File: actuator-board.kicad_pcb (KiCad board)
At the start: 2 copper layers, 60 parts, among them J1 SERVO PWR, M1 Motor_Servo, M2 Motor_Servo, M3 Pump 1, M4 Pump 2, U1 STM32F302K8U6, U2 MCP1703, U3 MAX3051, U4 MPRLS0015PA0000SA, U5 MPRLS0015PA0000SA, U6 DRV8847_TSSOP, X1 16MHz 10ppm

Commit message: Upadate footprints, rough arrangement
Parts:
- removed CONN5: ANALOG2, Connector_Molex:Molex_PicoBlade_53261-0271_1x02-1MP_P1.25mm_Horizontal
- removed CONN6: ANALOG1, Connector_Molex:Molex_PicoBlade_53261-0271_1x02-1MP_P1.25mm_Horizontal
- removed CONN7: Digital input 1, Connector_Molex:Molex_PicoBlade_53261-0271_1x02-1MP_P1.25mm_Horizontal
- removed L1: Solenoid 1, Connector_PinHeader_2.54mm:PinHeader_1x02_P2.54mm_Vertical
- removed L2: Solenoid 2, Connector_PinHeader_2.54mm:PinHeader_1x02_P2.54mm_Vertical
- removed M3: Pump 1, Connector_PinHeader_2.54mm:PinHeader_1x02_P2.54mm_Vertical
- removed M4: Pump 2, Connector_PinHeader_2.54mm:PinHeader_1x02_P2.54mm_Vertical
- added H1: MountingHole, MountingHole:MountingHole_2.2mm_M2, F.Cu at (50.8, 40.4)
- added H2: MountingHole, MountingHole:MountingHole_2.2mm_M2, F.Cu at (51.6, 102.4)
- added H3: MountingHole, MountingHole:MountingHole_2.2mm_M2, F.Cu at (87.6, 42.4)
- added H4: MountingHole, MountingHole:MountingHole_2.2mm_M2, F.Cu at (88.6, 102.6)
- added J2: Conn_01x06, Connector_Molex:Molex_PicoBlade_53261-0671_1x06-1MP_P1.25mm_Horizontal, F.Cu at (67.1, 102.4)
- added J3: Actuator1, Connector_Molex:Molex_PicoBlade_53261-0471_1x04-1MP_P1.25mm_Horizontal, F.Cu at (54.1, 49.8)
- added J4: Actuator2, Connector_Molex:Molex_PicoBlade_53261-0471_1x04-1MP_P1.25mm_Horizontal, F.Cu at (91.2, 50.8)
- C19: footprint Capacitor_THT:CP_Radial_D6.3mm_P2.50mm -> Capacitor_SMD:CP_Elec_5x5.8
- C2, C3, C4, C5, C6, C7, C8: footprint Capacitor_SMD:C_0402_1005Metric -> Capacitor_SMD:C_0603_1608Metric
- CONN3: footprint Connector_Molex:Molex_PicoBlade_53261-0471_1x04-1MP_P1.25mm_Horizontal -> Connector_Molex:Molex_PicoBlade_53398-0471_1x04-1MP_P1.25mm_Vertical
- CONN4: footprint Connector_Molex:Molex_PicoBlade_53261-0471_1x04-1MP_P1.25mm_Horizontal -> Connector_Molex:Molex_PicoBlade_53398-0471_1x04-1MP_P1.25mm_Vertical; moved to F.Cu
- J1: value SERVO PWR -> SERVO DCDC 5V; footprint Connector_PinHeader_2.54mm:PinHeader_1x02_P2.54mm_Vertical -> Connector_PinHeader_2.54mm:PinHeader_1x03_P2.54mm_Vertical
- M1, M2: footprint Connector_PinHeader_2.54mm:PinHeader_1x03_P2.54mm_Horizontal -> Connector_Molex:Molex_PicoBlade_53261-0371_1x03-1MP_P1.25mm_Horizontal
- moved C12 84.3 mm to (111.8, 133.9)
- moved R10 84.3 mm to (110.2, 136.9)
- moved R8 84.3 mm to (104.1, 133.3)
- moved C11 84.3 mm to (100.3, 135.1)
- moved R7 84.3 mm to (103.4, 136.7)
- moved R9 84.3 mm to (115.1, 135.1)
- moved M1 77.2 mm to (52.8, 61.7), turned to 270 degrees
- moved CONN4 64.4 mm to (90.7, 91.7)
- moved M2 60.2 mm to (90.4, 64.0), turned to 90 degrees
- moved C18 59.1 mm to (77.1, 37.2)
- moved D3 59.1 mm to (77.9, 34.3)
- moved D4 59.1 mm to (68.6, 41.5)
- moved D5 59.1 mm to (74.1, 41.5)
- moved R2 59.1 mm to (59.9, 44.6)
- moved C17 59.1 mm to (60.7, 41.7)
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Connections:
- J1 pad 1: Net-(C17-Pad1) -> +BATT

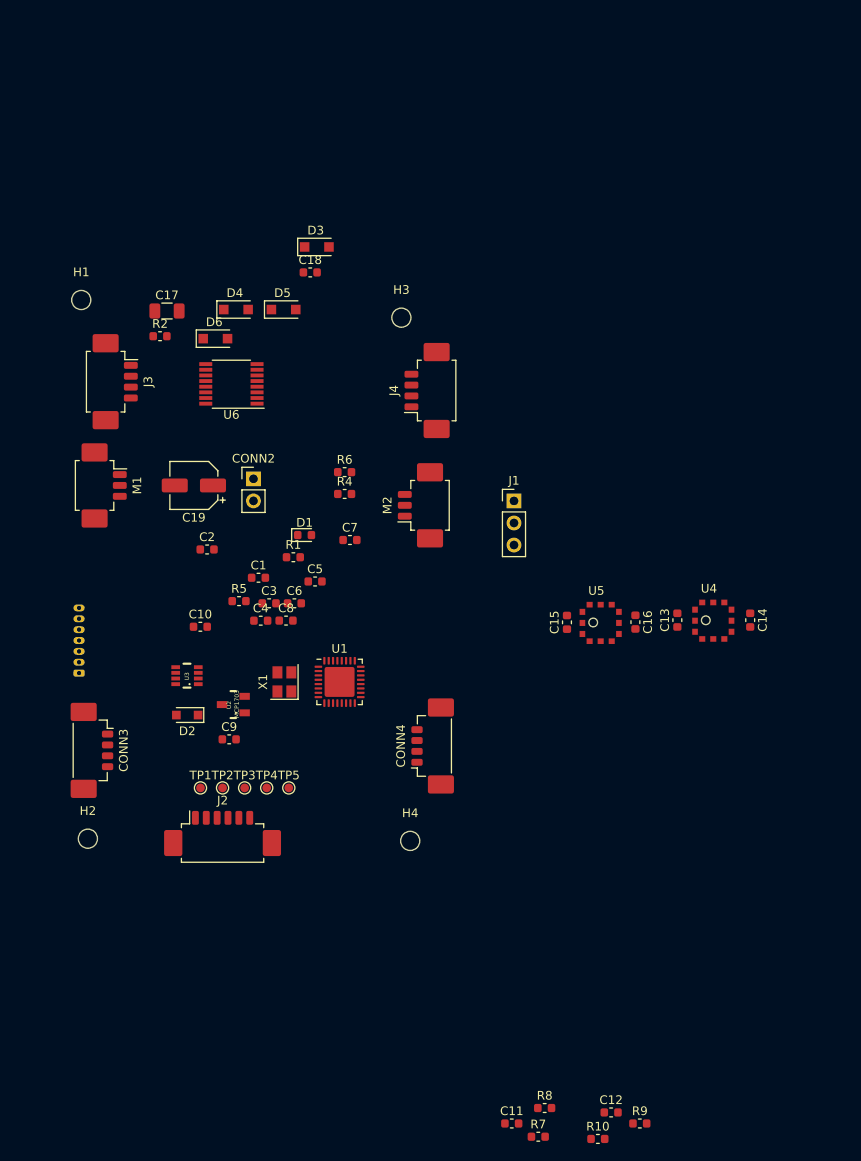
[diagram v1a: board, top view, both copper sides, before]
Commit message: Rough component placement, defined outline
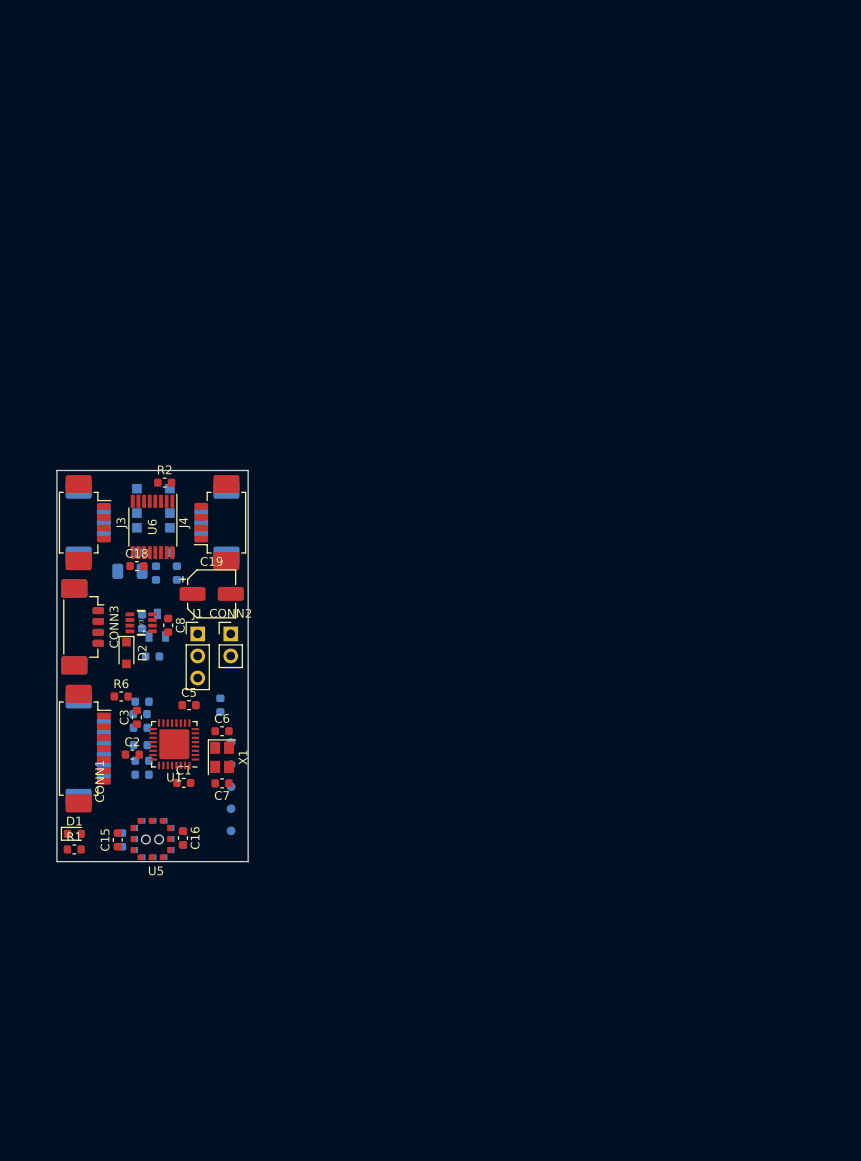
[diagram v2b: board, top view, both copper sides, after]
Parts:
- removed H1, H2, H3, H4: MountingHole, MountingHole:MountingHole_2.2mm_M2
- C10, C11, C12, C13, C14, C17, C4, C9, CONN4, D3, D4, D5, D6, J2, M1, M2, R10, R4, R5, R7, R8, R9, TP1, TP2, TP3, TP4, TP5, U2, U4: moved to B.Cu
- CONN1: footprint Connector_Molex:Molex_PicoBlade_53048-0710_1x07_P1.25mm_Horizontal -> Connector_Molex:Molex_PicoBlade_53261-0771_1x07-1MP_P1.25mm_Horizontal; moved to F.Cu
- moved R9 72.1 mm to (57.6, 91.6)
- moved U4 70.8 mm to (57.0, 104.5)
- moved C14 69.9 mm to (62.5, 102.3), turned to 90 degrees
- moved C13 68.7 mm to (55.5, 102.5), turned to 270 degrees
- moved R10 68.1 mm to (57.8, 93.4), turned to 180 degrees
- moved C12 66.5 mm to (57.8, 95.0), turned to 180 degrees
- moved R8 65.8 mm to (57.8, 86.6), turned to 180 degrees
- moved R7 65.6 mm to (57.6, 89.6), turned to 180 degrees
- moved C11 63.6 mm to (57.6, 88.0), turned to 180 degrees
- moved C16 57.7 mm to (62.5, 102.3)
- moved C15 57.4 mm to (55.0, 102.5)
- moved U5 55.6 mm to (61.0, 104.5), turned to 180 degrees
- moved D1 43.4 mm to (50.0, 101.8)
- moved R1 42.0 mm to (50.0, 103.6)
- moved CONN4 41.5 mm to (51.5, 78.0)
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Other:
- board outline added: 22 x 45 mm

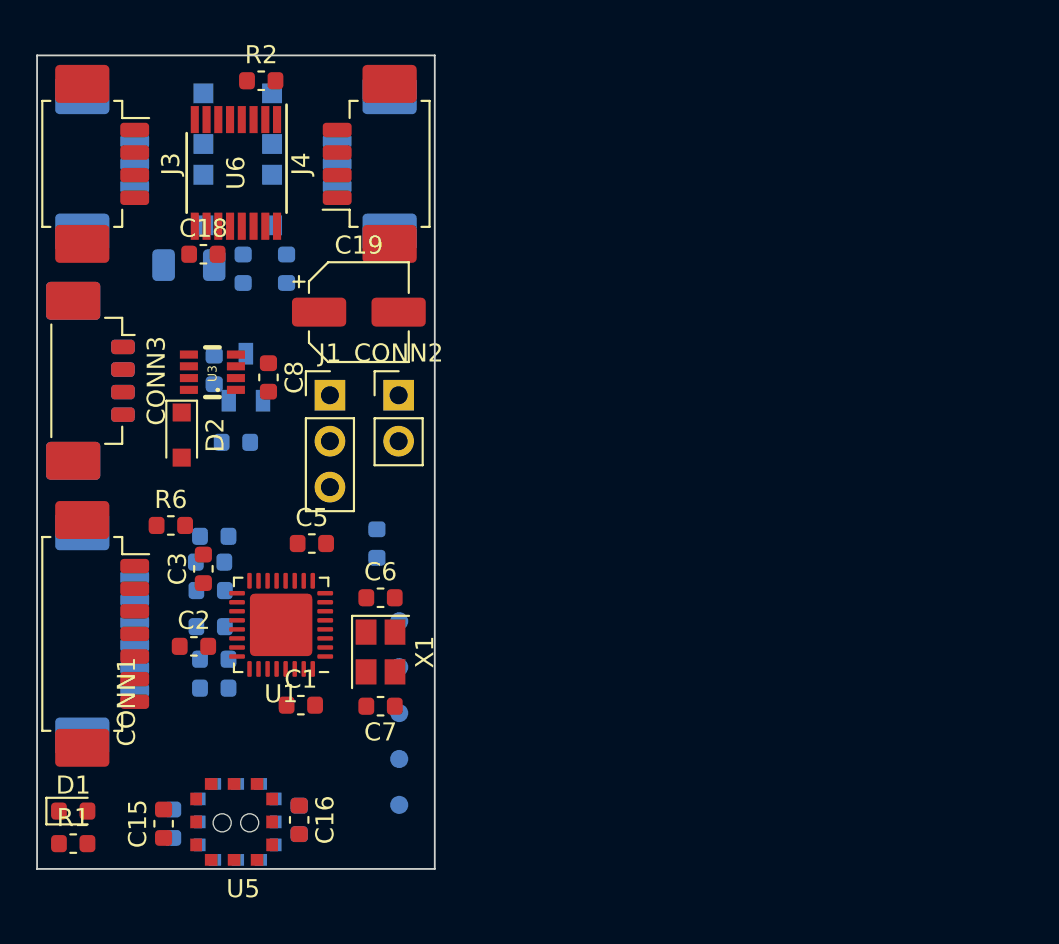
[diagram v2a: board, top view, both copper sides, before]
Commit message: Update footprints, better refdes, cleanup schematic, 40x22mm outline
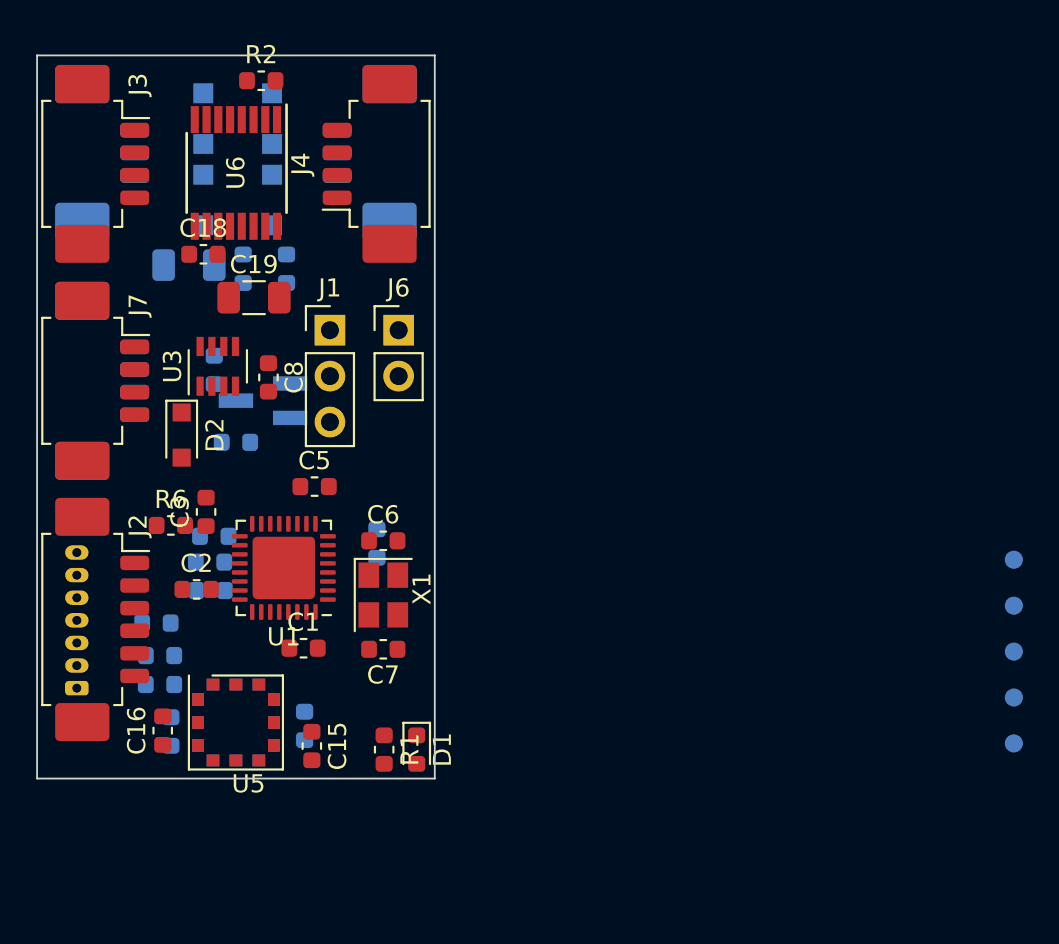
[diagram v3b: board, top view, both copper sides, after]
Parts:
- removed CONN1: SWD/DEBUG, Connector_Molex:Molex_PicoBlade_53261-0771_1x07-1MP_P1.25mm_Horizontal
- removed CONN2: BATTERY, Connector_PinHeader_2.54mm:PinHeader_1x02_P2.54mm_Vertical
- removed CONN3, CONN4: CAN, Connector_Molex:Molex_PicoBlade_53398-0471_1x04-1MP_P1.25mm_Vertical
- removed M1, M2: Motor_Servo, Connector_Molex:Molex_PicoBlade_53261-0371_1x03-1MP_P1.25mm_Horizontal
- added J10: Servo, Connector_Molex:Molex_PicoBlade_53261-0371_1x03-1MP_P1.25mm_Horizontal, B.Cu at (67.0, 65.4)
- added J5: SWD/DEBUG, Connector_Molex:Molex_PicoBlade_53047-0710_1x07_P1.25mm_Vertical, B.Cu at (50.2, 95.0)
- added J6: BATTERY, Connector_PinHeader_2.54mm:PinHeader_1x02_P2.54mm_Vertical, F.Cu at (68.0, 75.2)
- added J7: CAN, Connector_Molex:Molex_PicoBlade_53261-0471_1x04-1MP_P1.25mm_Horizontal, F.Cu at (51.0, 78.0)
- added J8: CAN, Connector_Molex:Molex_PicoBlade_53261-0471_1x04-1MP_P1.25mm_Horizontal, B.Cu at (51.0, 78.0)
- added J9: Servo, Connector_Molex:Molex_PicoBlade_53261-0371_1x03-1MP_P1.25mm_Horizontal, B.Cu at (51.0, 65.4)
- C10: value 22uF -> 1uF
- C18: value 0.1 uF -> 0.1uF
- C19: footprint Capacitor_SMD:CP_Elec_5x5.8 -> Capacitor_SMD:C_1206_3216Metric
- J2: moved to F.Cu
- U2: footprint _div:_MCP1703-SOT-23A -> Package_TO_SOT_SMD:SOT-23_Handsoldering
- U3: footprint _std:_SOT23-8 -> Package_TO_SOT_SMD:SOT-23-8
- U4, U5: footprint _sensors:MPR -> _sensors:MPR-AbsoluteRef
- moved TP1 34.2 mm to (102.0, 98.1)
- moved TP2 34.2 mm to (102.0, 95.5)
- moved TP3 34.2 mm to (102.0, 93.0)
- moved TP4 34.2 mm to (102.0, 90.4)
- moved TP5 34.2 mm to (102.0, 87.9)
- moved D1 19.3 mm to (69.0, 98.4), turned to 270 degrees
- moved R1 18.0 mm to (67.2, 98.4), turned to 270 degrees
- moved C15 9.26 mm to (63.2, 98.2), turned to 270 degrees
- moved C16 9.02 mm to (55.0, 97.3), turned to 90 degrees
- moved C19 5.85 mm to (60.0, 73.4)
- moved U4 5.50 mm to (56.9, 99.0)
- moved U5 5.50 mm to (61.1, 99.0)
- moved C14 5.21 mm to (62.8, 97.1)
- moved C13 5.10 mm to (55.4, 97.4)
- moved J1 3.60 mm to (64.2, 75.2)
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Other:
- board size 22 x 45 mm -> 22 x 40 mm
- copper layers 2 -> 4

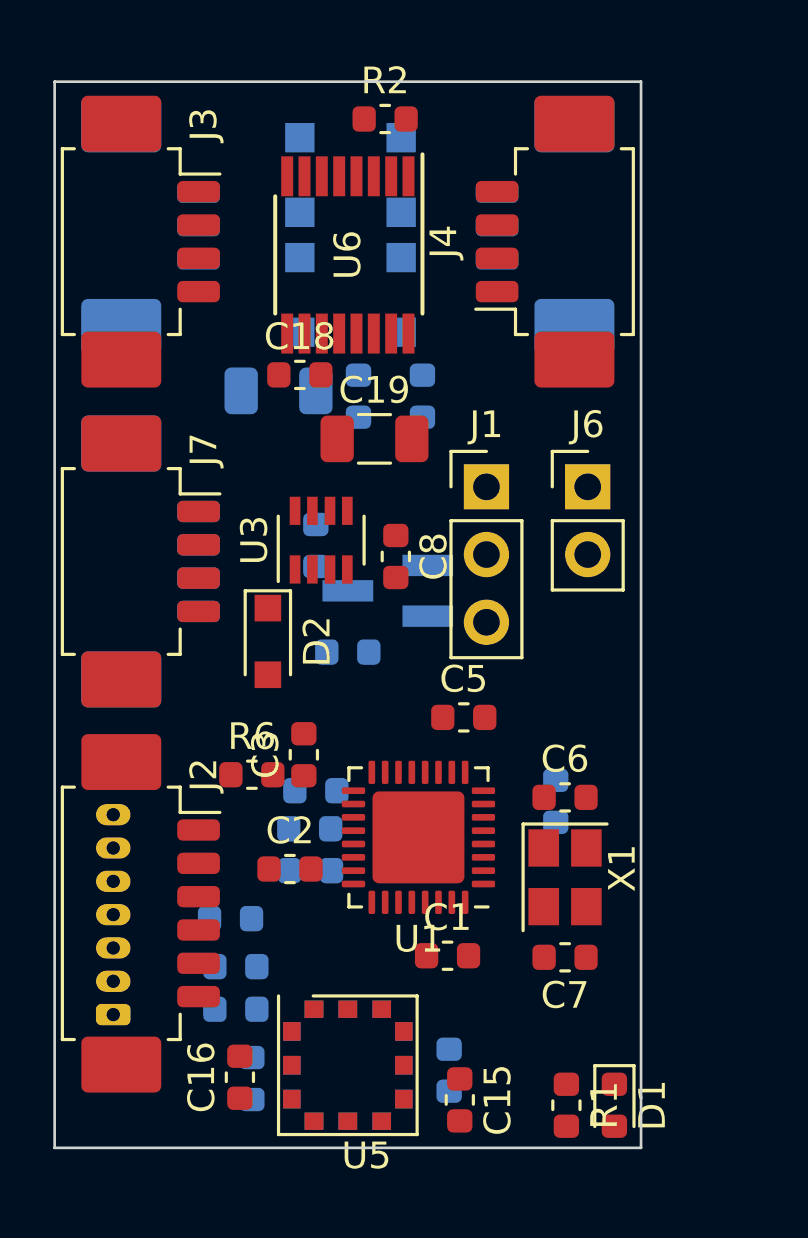
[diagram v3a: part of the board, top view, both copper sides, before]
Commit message: Update authors, DRC rules, layers, track/via settings
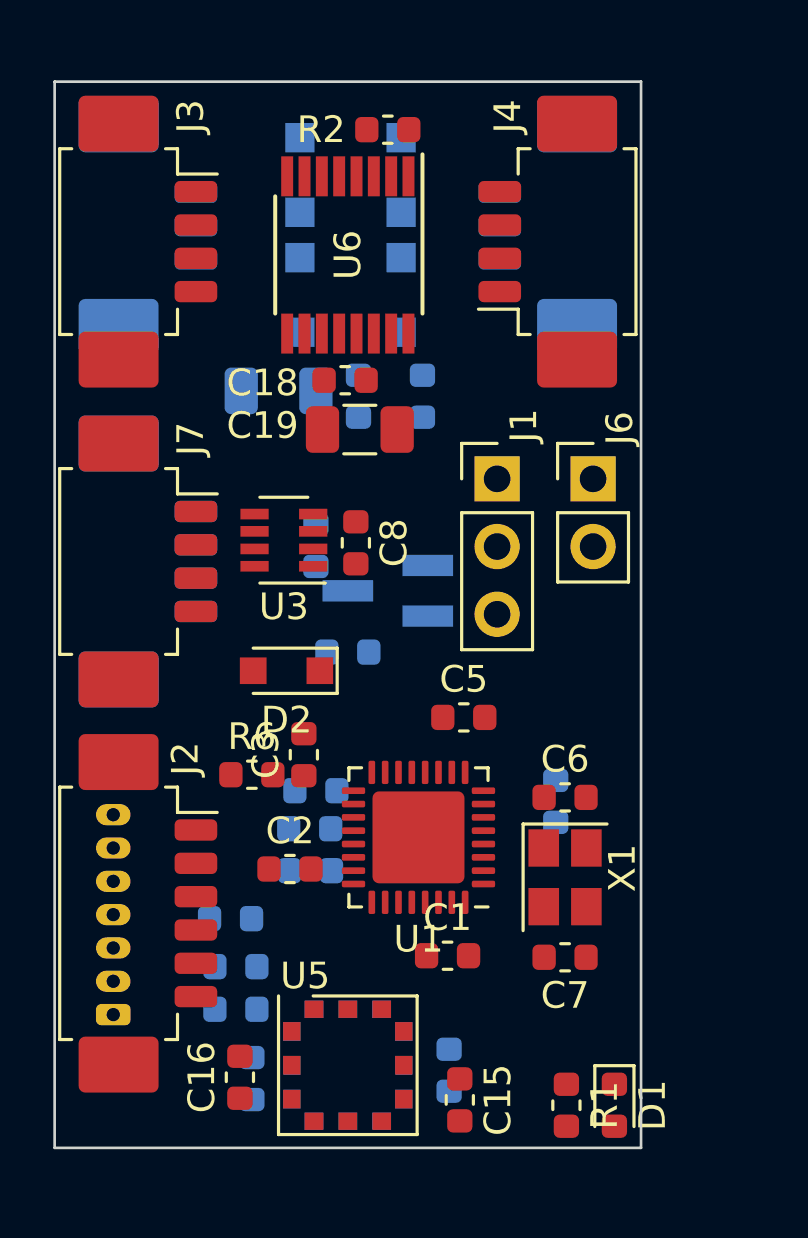
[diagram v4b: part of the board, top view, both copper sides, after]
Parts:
- moved C18 1.71 mm to (58.9, 71.2)
- moved C8 1.59 mm to (59.3, 77.3)
- moved U3 1.40 mm to (56.6, 77.2), turned to 180 degrees
- moved D2 1.30 mm to (56.7, 82.1), turned to 180 degrees
- moved C19 0.65 mm to (59.5, 73.0)
- moved J1 0.50 mm to (64.6, 74.9)
- moved R2 0.41 mm to (60.5, 61.8), turned to 180 degrees
- moved J6 0.36 mm to (68.2, 74.9)
- moved J2 0.10 mm to (50.9, 91.2)
- moved J3 0.10 mm to (50.9, 66.0)
- moved J7 0.10 mm to (50.9, 78.0)
- moved J8 0.10 mm to (50.9, 78.0)
- moved J9 0.10 mm to (50.9, 65.4)
- moved J10 0.10 mm to (67.1, 65.4)
- moved J4 0.10 mm to (67.1, 66.0)
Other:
- net class Default: clearance 0.2 -> 0.1524; trace_width 0.25 -> 0.1524; via_dia 0.8 -> 0.5; via_drill 0.4 -> 0.2
- rule pad_to_mask_clearance: 0 -> 0.05
- rule trace_clearance: 0.2 -> 0.1524
- rule trace_min: 0.2 -> 0.152
- rule via_min_drill: 0.3 -> 0.2
- rule via_min_size: 0.4 -> 0.5

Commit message: Sensor/gpio/debug routing
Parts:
- C11, C12, R10, R7, R8, R9: moved to F.Cu
- moved TP5 46.0 mm to (56.4, 93.3)
- moved TP3 44.3 mm to (57.7, 93.3)
- moved TP1 43.3 mm to (59.0, 93.3)
- moved TP4 41.8 mm to (60.3, 93.3)
- moved TP2 40.5 mm to (61.6, 93.3)
- moved C4 13.5 mm to (53.4, 88.2), turned to 90 degrees
- moved C3 8.18 mm to (65.5, 84.6), turned to 180 degrees
- moved C2 7.93 mm to (61.0, 82.8)
- moved J5 7.60 mm to (50.4, 87.4), turned to 270 degrees
- moved R6 7.40 mm to (55.4, 93.4), turned to 270 degrees
- moved C12 6.43 mm to (56.1, 88.5)
- moved C11 4.01 mm to (56.1, 84.3)
- moved R10 3.55 mm to (56.1, 89.9)
- moved C9 3.37 mm to (61.1, 76.7), turned to 0 degrees
- moved R7 2.92 mm to (56.1, 87.1), turned to 0 degrees
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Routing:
- net /VACUUM_SENS_RESET: track 0.00 -> 30.1 mm, vias 0 -> 2
- net /SPI_CS1: track 0.00 -> 18.9 mm, vias 0 -> 1
- net /SPI_MISO: track 0.00 -> 17.1 mm, vias 0 -> 3
- net /RESET: track 0.00 -> 17.0 mm, vias 0 -> 1
- net /UART1RX: track 0.00 -> 15.9 mm, vias 0 -> 2
- net /UART1TX: track 0.00 -> 15.8 mm, vias 0 -> 2
- net /ANALOG2: track 0.00 -> 13.0 mm, vias 0 -> 2
- net /CAN_TX: track 0.00 -> 12.9 mm
- net VCC: track 0.00 -> 12.2 mm
- net /SPI_SCK: track 0.00 -> 11.8 mm, vias 0 -> 1
- net /ANALOG1: track 0.00 -> 10.6 mm, vias 0 -> 2
- net /SPI_CS2: track 0.00 -> 8.84 mm, vias 0 -> 1
- net /SWIO: track 0.00 -> 8.54 mm, vias 0 -> 1
- net /SWCK: track 0.00 -> 8.34 mm, vias 0 -> 1
- net /SPI_MOSI: track 0.00 -> 8.16 mm
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- added copper zone on In1.Cu, net GND
- added copper zone on In2.Cu, net VCC
